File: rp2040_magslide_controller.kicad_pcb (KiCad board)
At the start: 4 copper layers, 36.1 x 66.8 mm, 49 parts, among them J1 USB_B_Mini, J2 50-00174, J3 Conn_02x05_Odd_Even, J4 Conn_02x20_Odd_Even, SW1 SW_SPST, SW2 SW_SPST, U1 W25Q64JV, U2 AMS1117-3.3, U3 RP2040, U4 CD74HC4067SM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

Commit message: Inc
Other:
- board text added: "By Philip K. Gisslow"
- board text added: "Magslide Controller RP2040 Rev. 1"
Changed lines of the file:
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@@
   (gr_arc (start 193.548 77.978) (mid 196.062472 79.019528) (end 197.104 81.534) (layer "Edge.Cuts") (width 0.1))
   (gr_line (start 161.036 141.224) (end 161.036 81.534) (layer "Edge.Cuts") (width 0.1))
+  (gr_text "Magslide Controller RP2040 Rev. 1" (at 170.1 130.5 270) (layer "F.SilkS")
+    (effects (font (size 1 1) (thickness 0.15)))
+  )
+  (gr_text "By Philip K. Gisslow" (at 167.9 136 270) (layer "F.SilkS")
+    (effects (font (size 1 1) (thickness 0.15)))
+  )
   (segment (start 184.747 86.145) (end 184.747 85.5598) (width 0.2) (layer "F.Cu") (net 1))
   (segment (start 171.200801 109.794184) (end 171.015 109.608383) (width 0.2) (layer "F.Cu") (net 1))

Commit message: Inc
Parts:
- moved J1 0.08 mm to (179.2, 80.7)

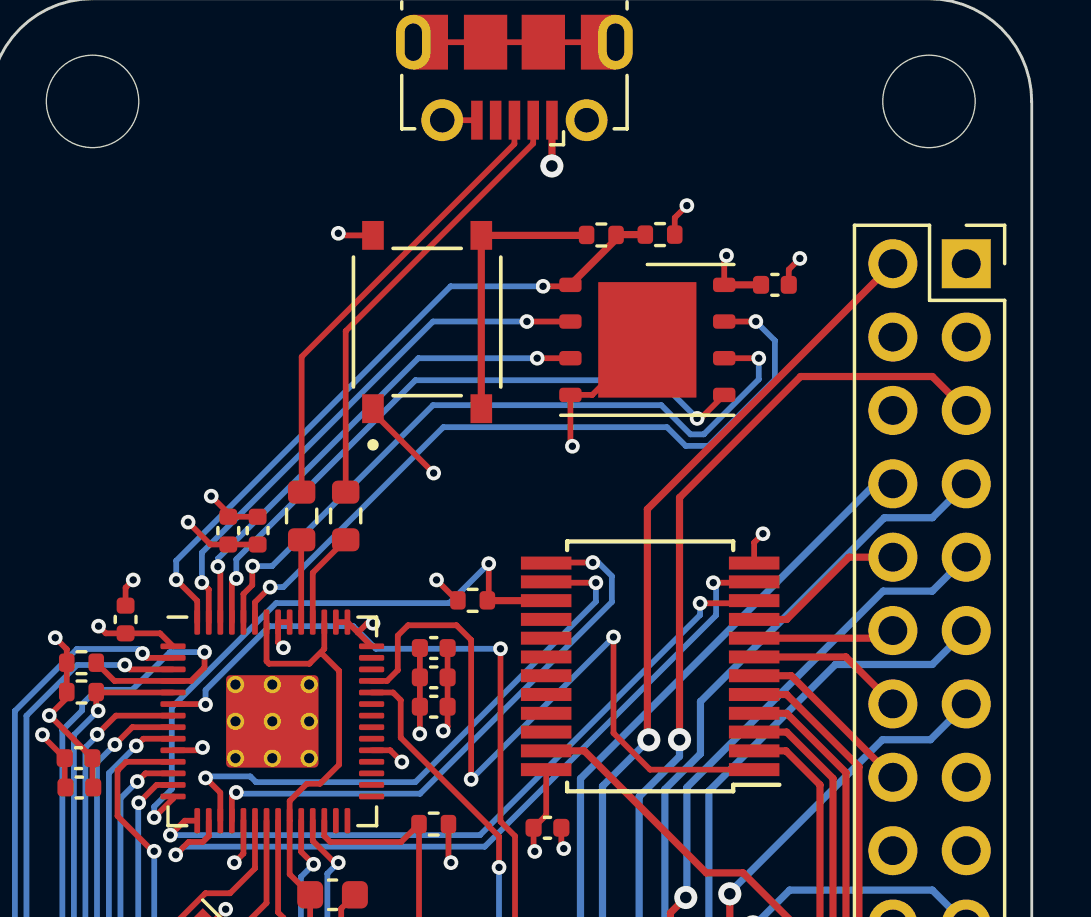
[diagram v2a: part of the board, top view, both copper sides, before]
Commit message: Adds SOP8 flash instead
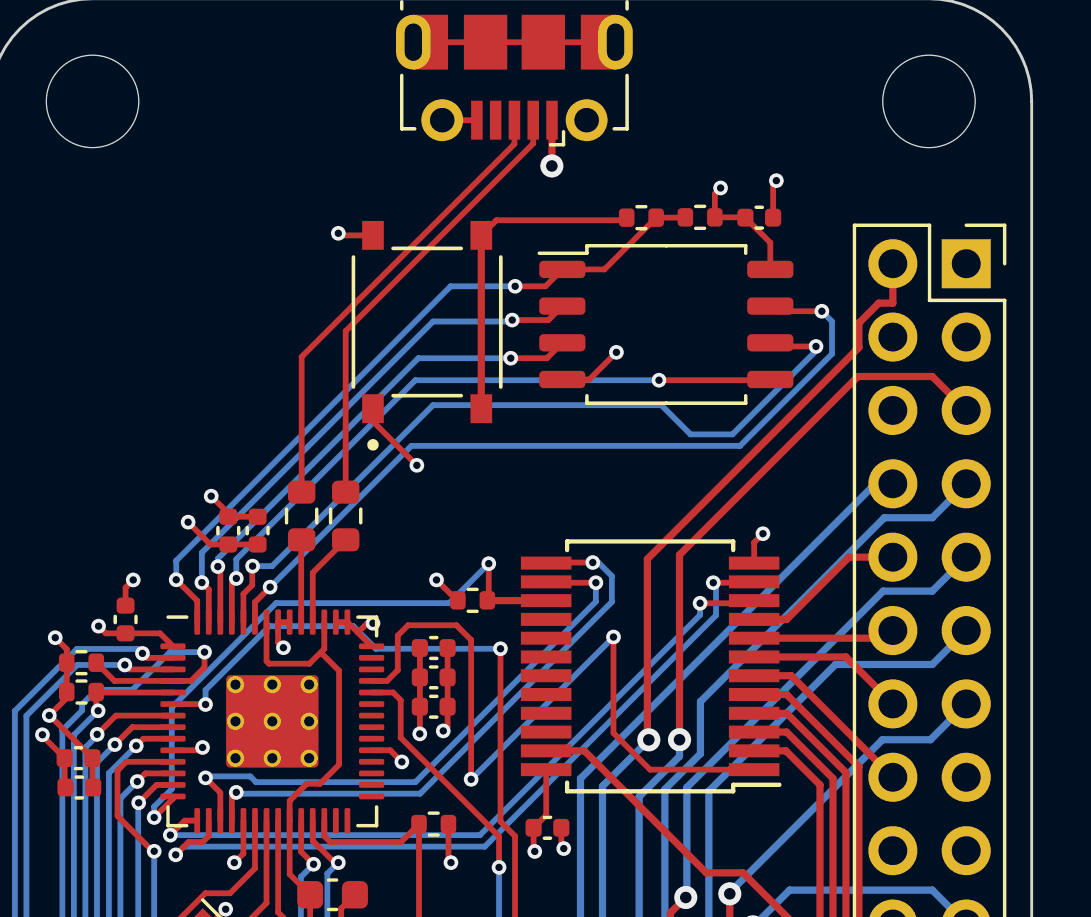
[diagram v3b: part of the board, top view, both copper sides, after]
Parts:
- U1: footprint Package_SON:WSON-8-1EP_6x5mm_P1.27mm_EP3.4x4mm -> Package_SO:SOP-8_5.28x5.23mm_P1.27mm
- moved C1 2.39 mm to (187.7, 85.6)
- moved R4 1.51 mm to (185.6, 85.5)
- moved R2 1.51 mm to (183.6, 85.6)
- moved U1 0.85 mm to (184.5, 89.3)
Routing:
- net GND: track 61.4 -> 58.1 mm
- net QSPI_SCLK: track 25.1 -> 27.4 mm
- net QSPI_SD3: track 25.8 -> 27.7 mm
- net Net-(R2-Pad1): track 9.65 -> 11.3 mm
- net QSPI_CS: track 23.4 -> 25.0 mm
- net F00: track 31.7 -> 30.6 mm
- net +3V3: track 47.9 -> 48.7 mm, vias 20 -> 19
- net QSPI_SD0: track 22.6 -> 23.3 mm

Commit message: Inc
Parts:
- removed H2, H3, H4: MountingHole, MountingHole:MountingHole_3.2mm_M3
- removed J4: Conn_02x20_Odd_Even, Connector_PinSocket_2.54mm:PinSocket_2x20_P2.54mm_Vertical
- removed R10, R11: 10k, Resistor_SMD:R_0402_1005Metric
- removed R8, R9: 27R 0603, Resistor_SMD:R_0603_1608Metric
- removed SW1, SW2: SW_SPST, local:SW_TS-1187A-B-A-B
- added S1: OH49E-S, Package_TO_SOT_SMD:SOT-23, F.Cu at (182.4, 118.0)
- added S2: OH49E-S, Package_TO_SOT_SMD:SOT-23, F.Cu at (178.6, 114.2)
- added S3: OH49E-S, Package_TO_SOT_SMD:SOT-23, F.Cu at (174.9, 118.0)
- added S4: OH49E-S, Package_TO_SOT_SMD:SOT-23, F.Cu at (178.6, 121.8)
- C18: value 100n -> 100nF; footprint Capacitor_SMD:C_0402_1005Metric -> Capacitor_SMD:C_0603_1608Metric
- C19: value 100n -> 10uF; footprint Capacitor_SMD:C_0402_1005Metric -> Capacitor_SMD:C_0603_1608Metric
- C2: value 4u7 -> 10uF
- C3, C7: value 1u -> 10uF
- C6: value 4u7 -> 100nF
- H1: footprint MountingHole:MountingHole_3.2mm_M3 -> magslide_keys:MagHole
- J1: value USB_B_Mini -> Pressure sensor; footprint Connector_USB:USB_Micro-B_Molex-105017-0001 -> Connector_PinHeader_1.00mm:PinHeader_1x02_P1.00mm_Vertical
- JP1: footprint Jumper:SolderJumper-2_P1.3mm_Open_TrianglePad1.0x1.5mm -> Jumper:SolderJumper-2_P1.3mm_Open_RoundedPad1.0x1.5mm
- JP2: value SolderJumper_2_Open -> SolderJumper_3_Open; footprint Jumper:SolderJumper-2_P1.3mm_Open_TrianglePad1.0x1.5mm -> Jumper:SolderJumper-3_P1.3mm_Open_RoundedPad1.0x1.5mm
- R2: value 1K -> 10k
- R5, R6: value 4.7k -> 10k
- U2: value AMS1117-3.3 -> AP2112K-3.3; footprint Package_TO_SOT_SMD:SOT-223-3_TabPin2 -> Package_TO_SOT_SMD:SOT-23-5
- U4: value CD74HC4067SM -> LIS3DH; footprint Package_SO:SSOP-24_5.3x8.2mm_P0.65mm -> Package_LGA:LGA-16_3x3mm_P0.5mm_LayoutBorder3x5y
- U5: value CD74HC4067SM -> SGM3157; footprint Package_SO:SSOP-24_5.3x8.2mm_P0.65mm -> misc:SC70-6
- moved C4 80.0 mm to (239.6, 81.7), turned to 0 degrees
- moved R5 75.3 mm to (236.7, 81.7)
- moved C16 68.9 mm to (233.7, 87.8), turned to 0 degrees
- moved R3 67.4 mm to (229.5, 90.2), turned to 0 degrees
- moved C2 66.9 mm to (233.3, 82.0), turned to 0 degrees
- moved C11 66.7 mm to (235.8, 84.2), turned to 0 degrees
- moved C13 65.1 mm to (238.7, 83.7)
- moved C5 64.3 mm to (230.8, 87.8), turned to 0 degrees
- moved J2 62.8 mm to (197.1, 85.4), turned to 0 degrees
- moved Y1 62.2 mm to (223.8, 83.0), turned to 0 degrees
- moved C7 58.9 mm to (212.8, 88.8), turned to 0 degrees
- moved C6 57.1 mm to (221.2, 95.3), turned to 0 degrees
- moved C9 56.2 mm to (226.1, 90.9)
- moved C17 53.9 mm to (218.0, 102.4), turned to 0 degrees
- moved C12 53.9 mm to (229.5, 92.2)
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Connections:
- J1 pad 1: +5V -> +3V3
- J1 pad 2: D- -> PRESSURE
- JP1 pad 1: Net-(JP1-Pad1) -> SENS4
- JP1 pad 2: board_scl -> Net-(JP1-Pad2)
- JP2 pad 1: Net-(JP2-Pad1) -> SENS4
- JP2 pad 2: board_sda -> ADC4
- R1 pad 2: Net-(JP1-Pad1) -> board_scl
- R2 pad 1: Net-(R2-Pad1) -> +3V3
- R2 pad 2: QSPI_CS -> Net-(U3-Pad4)
- R3 pad 2: Net-(JP2-Pad1) -> board_sda
- R5 pad 2: extern_scl -> Net-(U3-Pad5)
- R6 pad 1: +3V3 -> GND
- R6 pad 2: extern_sda -> PRESSURE
- U2 pad 1: GND -> +5V
- U2 pad 2: +3V3 -> GND
- U3 pad 11: MUX_01 -> unconnected-(U3-Pad11)
- U3 pad 12: MUX_02 -> unconnected-(U3-Pad12)
- U3 pad 13: MUX_03 -> ADC4_SEL
- U3 pad 14: MUX1_EN -> unconnected-(U3-Pad14)
- U3 pad 15: MUX_10 -> unconnected-(U3-Pad15)
- U3 pad 16: MUX_11 -> unconnected-(U3-Pad16)
- U3 pad 17: MUX_12 -> unconnected-(U3-Pad17)
- U3 pad 18: MUX_13 -> unconnected-(U3-Pad18)
- U3 pad 38: ADC_0 -> SENS1
- U3 pad 39: ADC_1 -> SENS2
- U3 pad 4: extern_sda -> Net-(U3-Pad4)
- U3 pad 40: unconnected-(U3-Pad40) -> SENS3
- U3 pad 41: unconnected-(U3-Pad41) -> ADC4
- U3 pad 46: Net-(R9-Pad1) -> unconnected-(U3-Pad46)
- U3 pad 47: Net-(R8-Pad1) -> unconnected-(U3-Pad47)
- U3 pad 5: extern_scl -> Net-(U3-Pad5)
- U3 pad 8: MUX0_EN -> unconnected-(U3-Pad8)
- U3 pad 9: MUX_00 -> unconnected-(U3-Pad9)
- U4 pad 1: ADC_0 -> +3V3
- U4 pad 10: MUX_00 -> GND
- U4 pad 11: MUX_01 -> unconnected-(U4-Pad11)
- U4 pad 13: MUX_03 -> unconnected-(U4-Pad13)
- U4 pad 14: MUX_02 -> +3V3
- U4 pad 15: MUX0_EN -> unconnected-(U4-Pad15)
- U4 pad 16: F30 -> unconnected-(U4-Pad16)
- U4 pad 2: F12 -> unconnected-(U4-Pad2)
- U4 pad 3: F11 -> unconnected-(U4-Pad3)
- U4 pad 4: F10 -> Net-(U3-Pad5)
- U4 pad 5: F04 -> GND
- U4 pad 6: F03 -> Net-(U3-Pad4)
- U4 pad 7: F02 -> GND
- U4 pad 8: F01 -> +3V3
- U4 pad 9: F00 -> unconnected-(U4-Pad9)
- U5 pad 1: ADC_1 -> PRESSURE
- U5 pad 2: F43 -> GND
- U5 pad 3: F42 -> Net-(JP1-Pad2)
- U5 pad 4: F41 -> MUX_OUT
- U5 pad 5: F40 -> +3V3
- U5 pad 6: F34 -> ADC4_SEL
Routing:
- net +5V: track 115.1 -> 0.00 mm, vias 3 -> 0
- net extern_sda: track 59.9 -> 0.00 mm, vias 2 -> 0
- net GND: track 58.1 -> 0.00 mm, vias 26 -> 0
- net board_sda: track 53.1 -> 0.00 mm, vias 3 -> 0
- net extern_scl: track 50.0 -> 0.00 mm, vias 2 -> 0
- net +3V3: track 48.7 -> 0.00 mm, vias 19 -> 0
- net board_scl: track 42.5 -> 0.00 mm, vias 2 -> 0
- net F24: track 38.6 -> 0.00 mm, vias 2 -> 0
- net MUX0_EN: track 35.7 -> 0.00 mm, vias 2 -> 0
- net F30: track 31.3 -> 0.00 mm, vias 1 -> 0
- net MUX_00: track 30.7 -> 0.00 mm, vias 4 -> 0
- net F00: track 30.6 -> 0.00 mm, vias 2 -> 0
- net MUX_02: track 30.3 -> 0.00 mm, vias 2 -> 0
- net dbg_tx: track 28.2 -> 0.00 mm, vias 2 -> 0
- net MUX_01: track 28.0 -> 0.00 mm, vias 2 -> 0
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- removed copper zone on In1.Cu, net +3V3
- removed copper zone on In2.Cu, net GND
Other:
- board size 36.1 x 66.8 mm -> 16 x 19 mm
- board text removed: "By Philip K. Gisslow"
- board text removed: "Magslide Controller RP2040 Rev. 1"

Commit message: Inc
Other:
- board size 16 x 19 mm -> 16 x 16 mm
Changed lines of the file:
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@@
       ))
   )
-  (gr_arc (start 176.64 107.707) (mid 176.847076 107.207076) (end 177.347 107) (layer "Edge.Cuts") (width 0.2))
-  (gr_arc (start 180.64 110.254033) (mid 178.64 126) (end 176.64 110.254033) (layer "Edge.Cuts") (width 0.2))
-  (gr_arc (start 179.933 107) (mid 180.432924 107.207076) (end 180.64 107.707) (layer "Edge.Cuts") (width 0.2))
-  (gr_line (start 176.64 110.254033) (end 176.64 107.707) (layer "Edge.Cuts") (width 0.2))
-  (gr_line (start 177.347 107) (end 179.933 107) (layer "Edge.Cuts") (width 0.2))
-  (gr_line (start 180.64 107.707) (end 180.64 110.254033) (layer "Edge.Cuts") (width 0.2))
+  (gr_arc (start 176.64 107.707) (mid 176.847076 107.207076) (end 177.347 107) (layer "Cmts.User") (width 0.2))
+  (gr_arc (start 180.64 110.254033) (mid 178.64 126) (end 176.64 110.254033) (layer "Cmts.User") (width 0.2))
+  (gr_arc (start 179.933 107) (mid 180.432924 107.207076) (end 180.64 107.707) (layer "Cmts.User") (width 0.2))
+  (gr_line (start 176.64 110.254033) (end 176.64 107.707) (layer "Cmts.User") (width 0.2))
+  (gr_line (start 177.347 107) (end 179.933 107) (layer "Cmts.User") (width 0.2))
+  (gr_line (start 180.64 107.707) (end 180.64 110.254033) (layer "Cmts.User") (width 0.2))
+  (gr_circle (center 178.65 118) (end 186.65 118) (layer "Edge.Cuts") (width 0.1) (fill none))
   (group "" (id 77a3b364-4c8d-4259-85bb-745950c993c8)
     (members

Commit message: WIP
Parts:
- removed C3: 10uF, Capacitor_SMD:C_0603_1608Metric
- removed C6: 100nF, Capacitor_SMD:C_0603_1608Metric
- removed R1, R3: 4.7k, Resistor_SMD:R_0402_1005Metric
- JP1, JP2: moved to B.Cu
- moved C4 67.3 mm to (175.2, 101.1)
- moved R5 65.2 mm to (172.3, 92.0)
- moved C2 59.2 mm to (174.2, 85.9), turned to -90 degrees
- moved C13 54.3 mm to (184.7, 89.1)
- moved U5 52.9 mm to (184.7, 106.9), turned to 90 degrees
- moved R2 52.5 mm to (172.3, 90.9)
- moved C5 51.3 mm to (181.4, 101.8)
- moved C11 51.3 mm to (184.7, 88.0)
- moved C16 51.3 mm to (182.4, 88.0)
- moved C1 49.2 mm to (184.1, 80.5)
- moved Y1 48.6 mm to (178.3, 100.2), turned to 135 degrees
- moved C15 46.9 mm to (172.3, 94.0), turned to 180 degrees
- moved C12 45.7 mm to (183.8, 94.0)
- moved J1 45.4 mm to (185.3, 103.1)
- moved C14 45.2 mm to (172.3, 89.8), turned to 180 degrees
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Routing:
- net +1V1: track 0.00 -> 18.8 mm, vias 0 -> 3
- net +3V3: track 0.00 -> 16.7 mm, vias 0 -> 1
- net QSPI_CS: track 0.00 -> 13.7 mm
- net QSPI_SCLK: track 0.00 -> 10.0 mm, vias 0 -> 2
- net QSPI_SD0: track 0.00 -> 9.91 mm
- net QSPI_SD3: track 0.00 -> 9.75 mm, vias 0 -> 2
- net QSPI_SD1: track 0.00 -> 7.56 mm
- net GND: track 0.00 -> 7.38 mm, vias 0 -> 3
- net +5V: track 0.00 -> 7.31 mm
- net Net-(C5-Pad2): track 0.00 -> 7.30 mm
- net Net-(C4-Pad2): track 0.00 -> 6.67 mm
- net QSPI_SD2: track 0.00 -> 5.67 mm
- net Net-(R7-Pad2): track 0.00 -> 5.22 mm, vias 0 -> 2
- net Net-(R2-Pad2): track 0.00 -> 2.54 mm
- net Net-(R5-Pad2): track 0.00 -> 2.25 mm
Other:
- board size 16 x 16 mm -> 16 x 58.9 mm

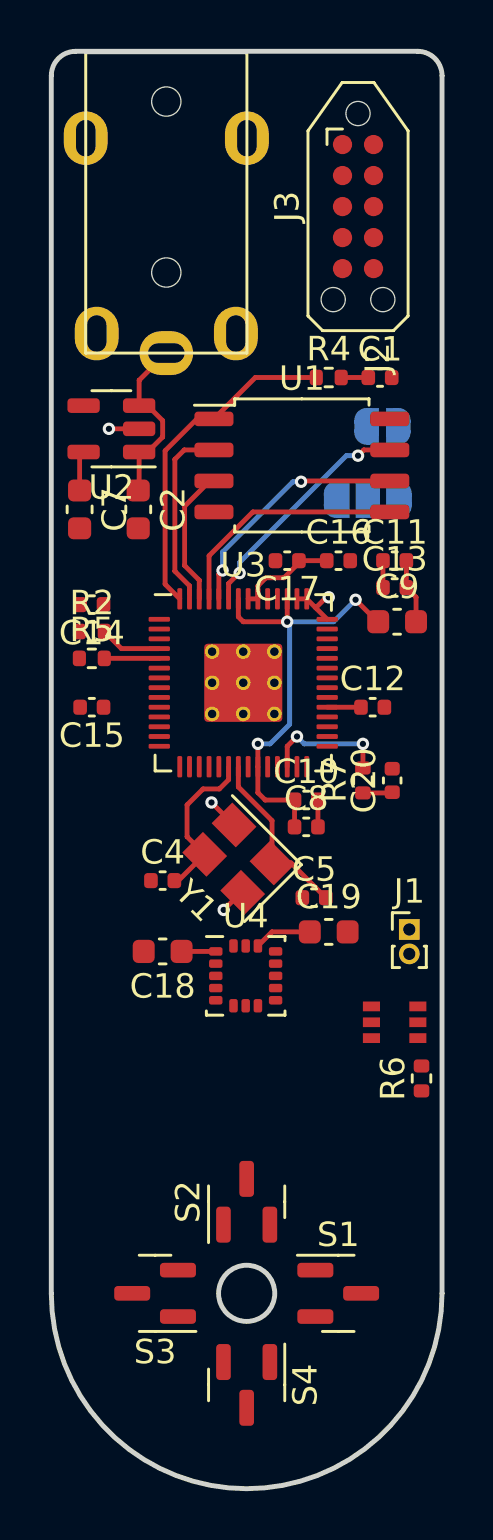
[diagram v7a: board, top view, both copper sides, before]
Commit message: Routing and DRC Done - Next up REVIEW
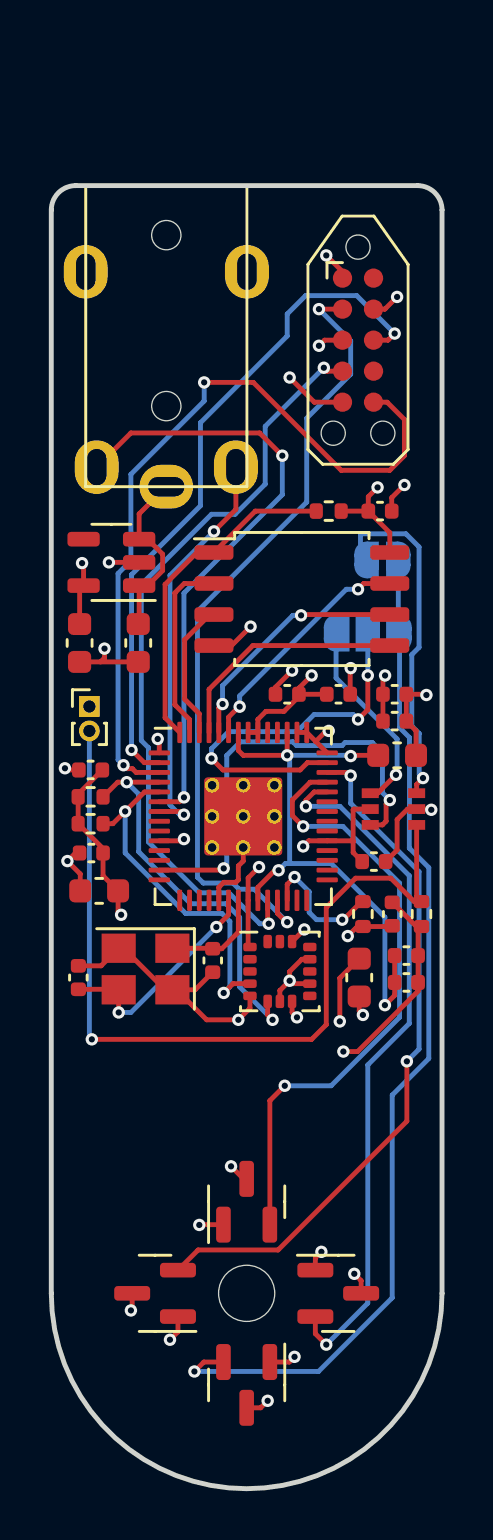
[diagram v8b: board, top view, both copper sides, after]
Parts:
- moved J1 16.0 mm to (172.2, 94.0)
- moved U5 8.73 mm to (184.7, 98.2)
- moved C10 7.58 mm to (185.2, 104.2)
- moved C8 7.58 mm to (185.2, 105.3)
- moved C14 6.77 mm to (172.2, 96.6)
- moved R2 6.77 mm to (172.2, 97.7)
- moved R5 6.77 mm to (172.2, 98.8)
- moved R6 6.73 mm to (185.8, 102.5)
- moved C12 6.32 mm to (183.8, 100.3)
- moved C15 5.97 mm to (172.3, 100.0)
- moved Y1 5.91 mm to (174.5, 104.7), turned to 180 degrees
- moved C1 5.47 mm to (184.1, 86.0)
- moved C11 5.47 mm to (184.7, 93.5)
- moved C13 5.47 mm to (184.7, 94.6)
- moved C16 5.47 mm to (182.4, 93.5)
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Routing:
- net GND: track 7.38 -> 56.1 mm, vias 3 -> 21
- net SENS4: track 0.00 -> 42.1 mm, vias 0 -> 1
- net PRESSURE: track 0.00 -> 35.3 mm, vias 0 -> 1
- net SWDIO: track 0.00 -> 32.9 mm, vias 0 -> 2
- net dbg_rx: track 0.00 -> 31.8 mm, vias 0 -> 2
- net SWCLK: track 0.00 -> 31.3 mm, vias 0 -> 2
- net SENS1: track 0.00 -> 28.6 mm, vias 0 -> 2
- net SENS3: track 0.00 -> 28.4 mm, vias 0 -> 2
- net dbg_tx: track 0.00 -> 28.2 mm, vias 0 -> 2
- net +3V3: track 16.7 -> 43.1 mm, vias 1 -> 19
- net board_sda: track 0.00 -> 25.3 mm, vias 0 -> 2
- net SENS2: track 0.00 -> 25.2 mm, vias 0 -> 2
- net ADC4_SEL: track 0.00 -> 17.9 mm, vias 0 -> 2
- net board_scl: track 0.00 -> 16.7 mm, vias 0 -> 2
- net ADC4: track 0.00 -> 15.8 mm, vias 0 -> 3
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- added copper zone on In1.Cu, net +3V3
- added copper zone on In2.Cu, net GND
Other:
- board size 16 x 58.9 mm -> 16 x 53.4 mm
